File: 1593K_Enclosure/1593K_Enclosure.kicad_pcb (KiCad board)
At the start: 2 copper layers, 56.6 x 57.7 mm, 5 parts

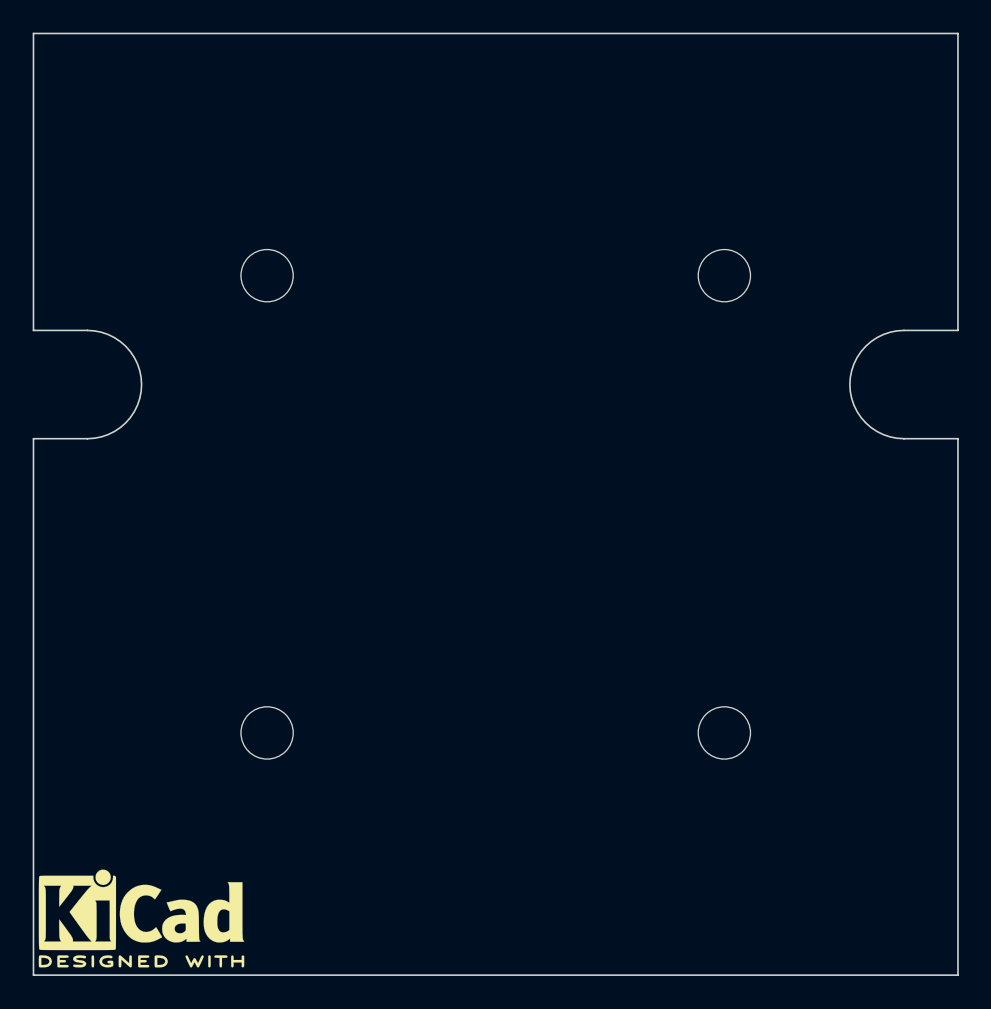
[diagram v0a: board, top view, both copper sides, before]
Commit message: Remap 1593K enclosure template
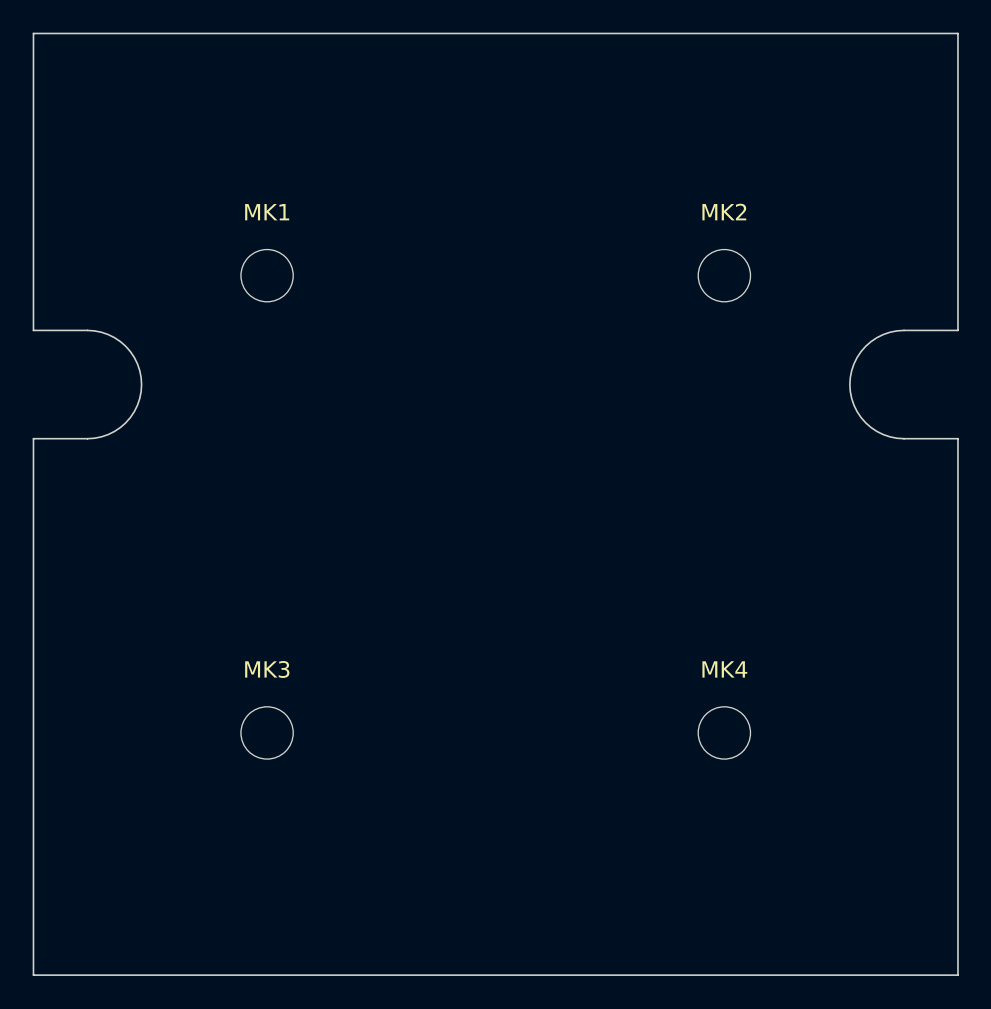
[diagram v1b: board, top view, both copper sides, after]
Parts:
- removed REF***: KiCad-Logo2_6mm_SilkScreen, Symbols:KiCad-Logo2_6mm_SilkScreen
- MK1, MK2, MK3, MK4: value MountingHole_3.2mm_M3_ISO14580 -> Mounting_Hole; footprint Mounting_Holes:MountingHole_3.2mm_M3_ISO14580 -> Mounting_Holes:MountingHole_3.2mm_M3_ISO7380
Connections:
- MK1 pad 1: (no net) -> Net-(MK1-Pad1)
- MK2 pad 1: (no net) -> Net-(MK2-Pad1)
- MK3 pad 1: (no net) -> Net-(MK3-Pad1)
- MK4 pad 1: (no net) -> Net-(MK4-Pad1)
